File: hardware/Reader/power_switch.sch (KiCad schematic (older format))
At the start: 9 parts

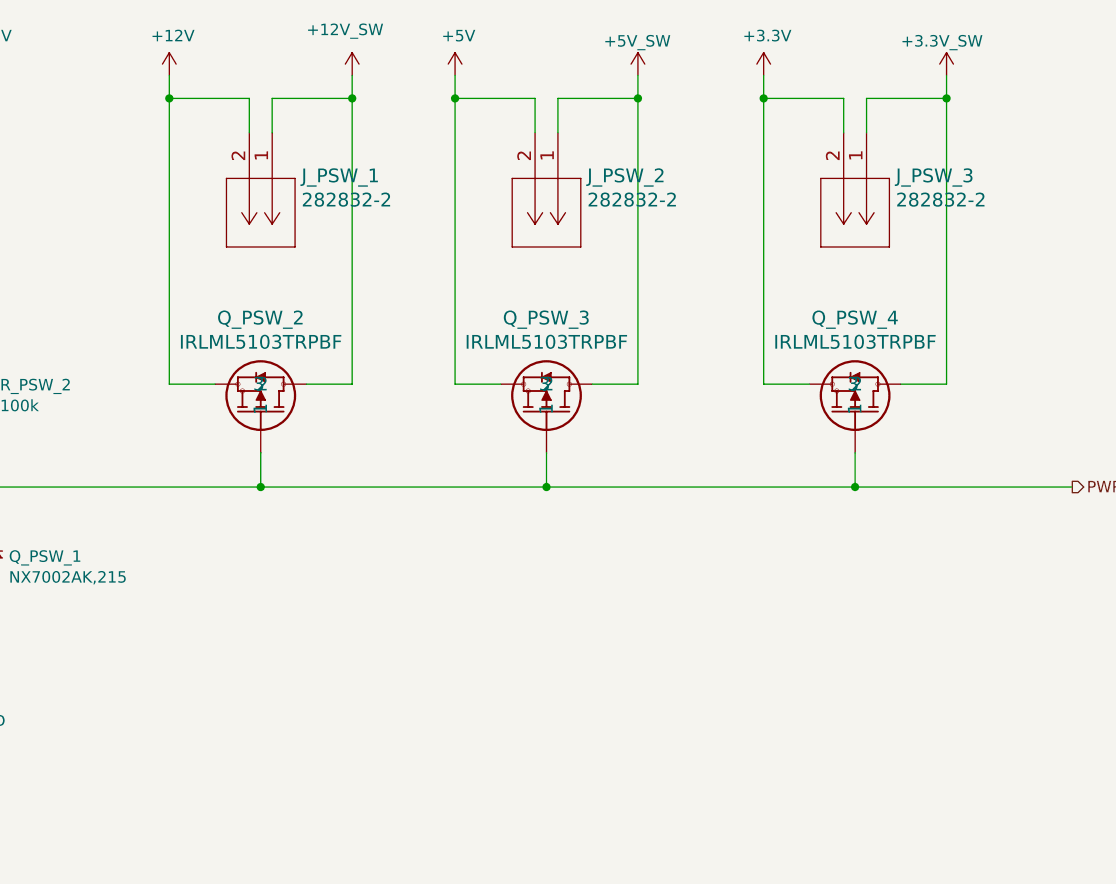
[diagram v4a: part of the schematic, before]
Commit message: Fixed bugs on the reader schematic. Exported Schematic Electrical report
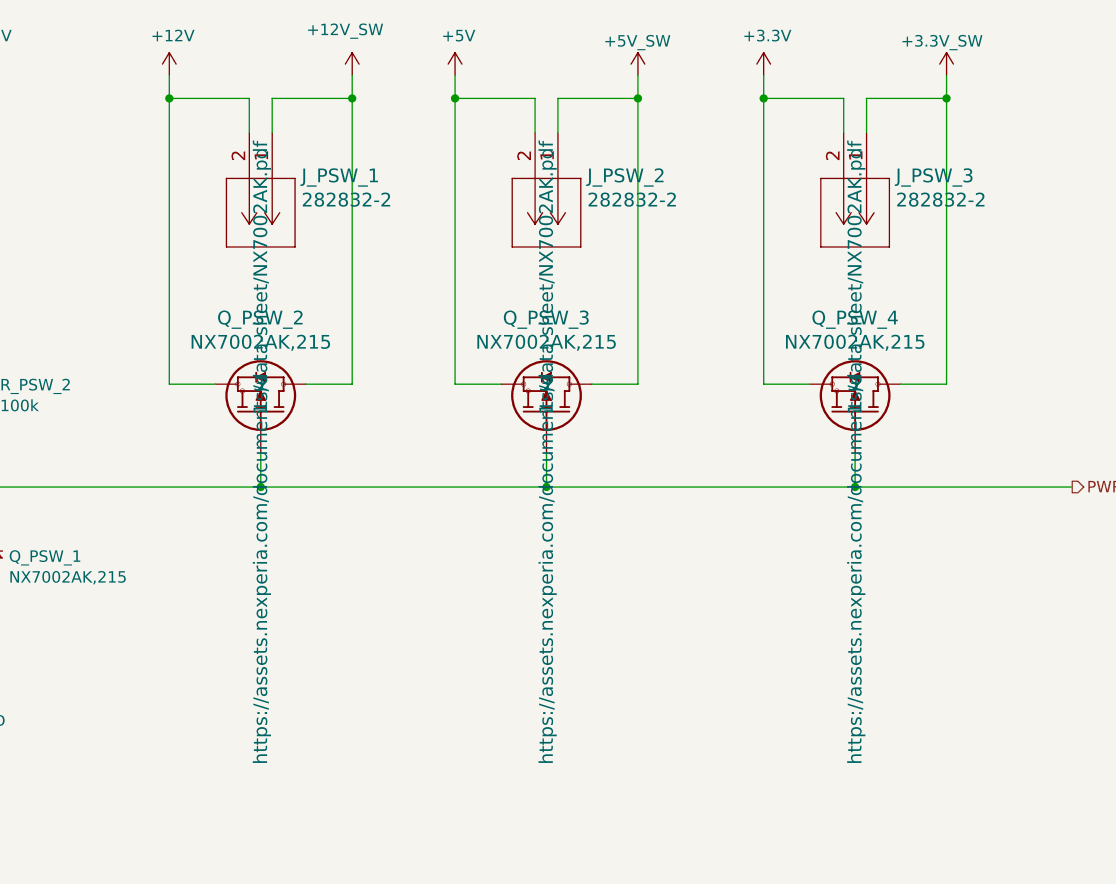
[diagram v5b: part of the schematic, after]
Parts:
- J_PSW_1, J_PSW_2, J_PSW_3: Manufacturer (none) -> TE Connectivity AMP Connectors; Vendor (none) -> DigiKey Canada; digikeypn (none) -> A113314-ND
- Q_PSW_1: Manufacturer (none) -> Nexperia USA Inc.; Part Name (none) -> NX7002AK,215; Vendor (none) -> DigiKey Canada; digikeypn (none) -> 1727-1289-1-ND
- Q_PSW_2, Q_PSW_3, Q_PSW_4: value IRLML5103TRPBF -> NX7002AK,215; footprint footprints:IRLML5103TRPBF -> footprints:SOT95P230X110-3N; Manufacturer (none) -> Nexperia USA Inc.; Part Name (none) -> NX7002AK,215; Vendor (none) -> DigiKey Canada; digikeypn (none) -> 1727-1289-1-ND
- R_PSW_1, R_PSW_2: Manufacturer (none) -> Yageo; Vendor (none) -> DigiKey Canada; digikeypn (none) -> 311-2395-1-ND
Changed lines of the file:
@@
 AR Path="/5FA56A4E/5FA57921" Ref="Q_PSW_3"  Part="1"
 F 0 "Q_PSW_3" V 6489 3500 60  0000 C CNN
-F 1 "IRLML5103TRPBF" V 6383 3500 60  0000 C CNN
-F 2 "footprints:IRLML5103TRPBF" H 6350 3240 60  0001 C CNN
-F 3 "" H 5900 3500 60  0000 C CNN
+F 1 "NX7002AK,215" V 6383 3500 60  0000 C CNN
+F 2 "footprints:SOT95P230X110-3N" H 6350 3240 60  0001 C CNN
+F 3 "https://assets.nexperia.com/documents/data-sheet/NX7002AK.pdf" H 5900 3500 60  0000 C CNN
+F 4 "NX7002AK,215" H 5900 3500 50  0001 C CNN "Part Name"
+F 5 "Nexperia USA Inc." H 5900 3500 50  0001 C CNN "Manufacturer"
+F 6 "DigiKey Canada" H 5900 3500 50  0001 C CNN "Vendor"
+F 7 "1727-1289-1-ND" H 5900 3500 50  0001 C CNN "digikeypn"
 	1    5900 3500
 	0    1    -1   0
@@
 AR Path="/5FA56A4E/5FA57927" Ref="Q_PSW_4"  Part="1"
 F 0 "Q_PSW_4" V 7839 3500 60  0000 C CNN
-F 1 "IRLML5103TRPBF" V 7733 3500 60  0000 C CNN
-F 2 "footprints:IRLML5103TRPBF" H 7700 3240 60  0001 C CNN
-F 3 "" H 7250 3500 60  0000 C CNN
+F 1 "NX7002AK,215" V 7733 3500 60  0000 C CNN
+F 2 "footprints:SOT95P230X110-3N" H 7700 3240 60  0001 C CNN
+F 3 "https://assets.nexperia.com/documents/data-sheet/NX7002AK.pdf" H 7250 3500 60  0000 C CNN
+F 4 "NX7002AK,215" H 7250 3500 50  0001 C CNN "Part Name"
+F 5 "Nexperia USA Inc." H 7250 3500 50  0001 C CNN "Manufacturer"
+F 6 "DigiKey Canada" H 7250 3500 50  0001 C CNN "Vendor"
+F 7 "1727-1289-1-ND" H 7250 3500 50  0001 C CNN "digikeypn"
 	1    7250 3500
 	0    1    -1   0
@@
 F 5 "7" H 3350 3950 50  0001 L BNN "Field5"
 F 6 "IPC-7351B" H 3350 3950 50  0001 L BNN "Field6"
+F 7 "NX7002AK,215" H 3350 3950 50  0001 C CNN "Part Name"
+F 8 "Nexperia USA Inc." H 3350 3950 50  0001 C CNN "Manufacturer"
+F 9 "DigiKey Canada" H 3350 3950 50  0001 C CNN "Vendor"
+F 10 "1727-1289-1-ND" H 3350 3950 50  0001 C CNN "digikeypn"
 	1    3350 3950
 	1    0    0    -1
@@
 F 1 "100k" H 3509 3205 50  0000 L CNN
 F 2 "footprints:RESC1608X55N" H 3450 3250 50  0001 C CNN
-F 3 "https://assets.nexperia.com/documents/data-sheet/NX7002AK.pdf" H 3450 3250 50  0001 C CNN
+F 3 "https://www.yageo.com/upload/media/product/productsearch/datasheet/rchip/PYu-RT_1-to-0.01_RoHS_L_12.pdf" H 3450 3250 50  0001 C CNN
 F 4 "RT0603DRE07100KL" H 3450 3250 50  0001 C CNN "Part Name"
+F 5 "Yageo" H 3450 3250 50  0001 C CNN "Manufacturer"
+F 6 "DigiKey Canada" H 3450 3250 50  0001 C CNN "Vendor"
+F 7 "311-2395-1-ND" H 3450 3250 50  0001 C CNN "digikeypn"
 	1    3450 3250
 	1    0    0    -1
@@
 F 1 "100k" H 2409 3505 50  0000 L CNN
 F 2 "footprints:RESC1608X55N" H 2350 3550 50  0001 C CNN
-F 3 "https://assets.nexperia.com/documents/data-sheet/NX7002AK.pdf" H 2350 3550 50  0001 C CNN
+F 3 "https://www.yageo.com/upload/media/product/productsearch/datasheet/rchip/PYu-RT_1-to-0.01_RoHS_L_12.pdf" H 2350 3550 50  0001 C CNN
 F 4 "RT0603DRE07100KL" H 2350 3550 50  0001 C CNN "Part Name"
+F 5 "Yageo" H 2350 3550 50  0001 C CNN "Manufacturer"
+F 6 "DigiKey Canada" H 2350 3550 50  0001 C CNN "Vendor"
+F 7 "311-2395-1-ND" H 2350 3550 50  0001 C CNN "digikeypn"
 	1    2350 3550
 	1    0    0    -1
@@
 AR Path="/5FA56A4E/5FA5791B" Ref="Q_PSW_2"  Part="1"
 F 0 "Q_PSW_2" V 5239 3500 60  0000 C CNN
-F 1 "IRLML5103TRPBF" V 5133 3500 60  0000 C CNN
-F 2 "footprints:IRLML5103TRPBF" H 5100 3240 60  0001 C CNN
-F 3 "" H 4650 3500 60  0000 C CNN
+F 1 "NX7002AK,215" V 5133 3500 60  0000 C CNN
+F 2 "footprints:SOT95P230X110-3N" H 5100 3240 60  0001 C CNN
+F 3 "https://assets.nexperia.com/documents/data-sheet/NX7002AK.pdf" H 4650 3500 60  0000 C CNN
+F 4 "NX7002AK,215" H 4650 3500 50  0001 C CNN "Part Name"
+F 5 "Nexperia USA Inc." H 4650 3500 50  0001 C CNN "Manufacturer"
+F 6 "DigiKey Canada" H 4650 3500 50  0001 C CNN "Vendor"
+F 7 "1727-1289-1-ND" H 4650 3500 50  0001 C CNN "digikeypn"
 	1    4650 3500
 	0    1    -1   0
@@
 F 3 "https://www.te.com/commerce/DocumentDelivery/DDEController?Action=srchrtrv&DocNm=282832&DocType=Customer+Drawing&DocLang=English" H 4700 2100 60  0001 C CNN
 F 4 "282832-2" H 4700 2100 50  0001 C CNN "Part Name"
+F 5 "DigiKey Canada" H 4700 2100 50  0001 C CNN "Vendor"
+F 6 "TE Connectivity AMP Connectors" H 4700 2100 50  0001 C CNN "Manufacturer"
+F 7 "A113314-ND" H 4700 2100 50  0001 C CNN "digikeypn"
 	1    4700 2100
 	0    1    1    0
@@
 F 3 "https://www.te.com/commerce/DocumentDelivery/DDEController?Action=srchrtrv&DocNm=282832&DocType=Customer+Drawing&DocLang=English" H 5950 2100 60  0001 C CNN
 F 4 "282832-2" H 5950 2100 50  0001 C CNN "Part Name"
+F 5 "DigiKey Canada" H 5950 2100 50  0001 C CNN "Vendor"
+F 6 "TE Connectivity AMP Connectors" H 5950 2100 50  0001 C CNN "Manufacturer"
+F 7 "A113314-ND" H 5950 2100 50  0001 C CNN "digikeypn"
 	1    5950 2100
 	0    1    1    0
@@
 F 3 "https://www.te.com/commerce/DocumentDelivery/DDEController?Action=srchrtrv&DocNm=282832&DocType=Customer+Drawing&DocLang=English" H 7300 2100 60  0001 C CNN
 F 4 "282832-2" H 7300 2100 50  0001 C CNN "Part Name"
+F 5 "DigiKey Canada" H 7300 2100 50  0001 C CNN "Vendor"
+F 6 "TE Connectivity AMP Connectors" H 7300 2100 50  0001 C CNN "Manufacturer"
+F 7 "A113314-ND" H 7300 2100 50  0001 C CNN "digikeypn"
 	1    7300 2100
 	0    1    1    0

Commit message: Fixed bugs in schematic. Updated BOM list. Swapped to using ESP32 holder. Updated PCB layout to v0.0.2. Updated schematic to v0.0.4
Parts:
- J_PSW_1, J_PSW_2, J_PSW_3: value 282832-2 -> 1546931-2; footprint footprints:282832-2 -> footprints:1546931-2; symbol 2828322:282832-2 -> Reader-rescue:282832-2-2828322; Part Name 282832-2 -> 1546931-2; digikeypn A113314-ND -> A97965-ND
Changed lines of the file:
@@
 Sheet 2 19
 Title "CANnect Reader | Power Switch"
-Date "2020-10-27"
-Rev "0.0.03"
+Date "2020-10-28"
+Rev "0.0.04"
 Comp "CANtech"
 Comment1 "Created by Choong Jin Ng | jin8383@gmail.com"
@@
 F 1 "NX7002AK,215" V 6383 3500 60  0000 C CNN
 F 2 "footprints:SOT95P230X110-3N" H 6350 3240 60  0001 C CNN
-F 3 "https://assets.nexperia.com/documents/data-sheet/NX7002AK.pdf" H 5900 3500 60  0000 C CNN
+F 3 "https://assets.nexperia.com/documents/data-sheet/NX7002AK.pdf" H 5900 3500 60  0001 C CNN
 F 4 "NX7002AK,215" H 5900 3500 50  0001 C CNN "Part Name"
 F 5 "Nexperia USA Inc." H 5900 3500 50  0001 C CNN "Manufacturer"
@@
 F 1 "NX7002AK,215" V 7733 3500 60  0000 C CNN
 F 2 "footprints:SOT95P230X110-3N" H 7700 3240 60  0001 C CNN
-F 3 "https://assets.nexperia.com/documents/data-sheet/NX7002AK.pdf" H 7250 3500 60  0000 C CNN
+F 3 "https://assets.nexperia.com/documents/data-sheet/NX7002AK.pdf" H 7250 3500 60  0001 C CNN
 F 4 "NX7002AK,215" H 7250 3500 50  0001 C CNN "Part Name"
 F 5 "Nexperia USA Inc." H 7250 3500 50  0001 C CNN "Manufacturer"
@@
 F 1 "NX7002AK,215" V 5133 3500 60  0000 C CNN
 F 2 "footprints:SOT95P230X110-3N" H 5100 3240 60  0001 C CNN
-F 3 "https://assets.nexperia.com/documents/data-sheet/NX7002AK.pdf" H 4650 3500 60  0000 C CNN
+F 3 "https://assets.nexperia.com/documents/data-sheet/NX7002AK.pdf" H 4650 3500 60  0001 C CNN
 F 4 "NX7002AK,215" H 4650 3500 50  0001 C CNN "Part Name"
 F 5 "Nexperia USA Inc." H 4650 3500 50  0001 C CNN "Manufacturer"
@@
 Connection ~ 7250 3650
 $Comp
-L 2828322:282832-2 J_PSW_1
+L Reader-rescue:282832-2-2828322 J_PSW_1
 U 1 1 5F9A0984
 P 4700 2100
+AR Path="/5F9A0984" Ref="J_PSW_1"  Part="1"
+AR Path="/5FA56A4E/5F9A0984" Ref="J_PSW_1"  Part="1"
 F 0 "J_PSW_1" V 4889 2228 60  0000 L CNN
-F 1 "282832-2" V 4995 2228 60  0000 L CNN
-F 2 "footprints:282832-2" H 5100 2040 60  0001 C CNN
-F 3 "https://www.te.com/commerce/DocumentDelivery/DDEController?Action=srchrtrv&DocNm=282832&DocType=Customer+Drawing&DocLang=English" H 4700 2100 60  0001 C CNN
-F 4 "282832-2" H 4700 2100 50  0001 C CNN "Part Name"
+F 1 "1546931-2" V 4995 2228 60  0000 L CNN
+F 2 "footprints:1546931-2" H 5100 2040 60  0001 C CNN
+F 3 "https://www.te.com/commerce/DocumentDelivery/DDEController?Action=srchrtrv&DocNm=1-1773458-1_EURO_STYLE_QRG&DocType=DS&DocLang=English" H 4700 2100 60  0001 C CNN
+F 4 "1546931-2" H 4700 2100 50  0001 C CNN "Part Name"
 F 5 "DigiKey Canada" H 4700 2100 50  0001 C CNN "Vendor"
 F 6 "TE Connectivity AMP Connectors" H 4700 2100 50  0001 C CNN "Manufacturer"
-F 7 "A113314-ND" H 4700 2100 50  0001 C CNN "digikeypn"
+F 7 "A97965-ND" H 4700 2100 50  0001 C CNN "digikeypn"
 	1    4700 2100
 	0    1    1    0
@@
 $EndComp
 $Comp
-L 2828322:282832-2 J_PSW_2
+L Reader-rescue:282832-2-2828322 J_PSW_2
 U 1 1 5F9A6466
 P 5950 2100
+AR Path="/5F9A6466" Ref="J_PSW_2"  Part="1"
+AR Path="/5FA56A4E/5F9A6466" Ref="J_PSW_2"  Part="1"
 F 0 "J_PSW_2" V 6139 2228 60  0000 L CNN
-F 1 "282832-2" V 6245 2228 60  0000 L CNN
-F 2 "footprints:282832-2" H 6350 2040 60  0001 C CNN
-F 3 "https://www.te.com/commerce/DocumentDelivery/DDEController?Action=srchrtrv&DocNm=282832&DocType=Customer+Drawing&DocLang=English" H 5950 2100 60  0001 C CNN
-F 4 "282832-2" H 5950 2100 50  0001 C CNN "Part Name"
+F 1 "1546931-2" V 6245 2228 60  0000 L CNN
+F 2 "footprints:1546931-2" H 6350 2040 60  0001 C CNN
+F 3 "https://www.te.com/commerce/DocumentDelivery/DDEController?Action=srchrtrv&DocNm=1-1773458-1_EURO_STYLE_QRG&DocType=DS&DocLang=English" H 5950 2100 60  0001 C CNN
+F 4 "1546931-2" H 5950 2100 50  0001 C CNN "Part Name"
 F 5 "DigiKey Canada" H 5950 2100 50  0001 C CNN "Vendor"
 F 6 "TE Connectivity AMP Connectors" H 5950 2100 50  0001 C CNN "Manufacturer"
-F 7 "A113314-ND" H 5950 2100 50  0001 C CNN "digikeypn"
+F 7 "A97965-ND" H 5950 2100 50  0001 C CNN "digikeypn"
 	1    5950 2100
 	0    1    1    0
 $EndComp
 $Comp
-L 2828322:282832-2 J_PSW_3
+L Reader-rescue:282832-2-2828322 J_PSW_3
 U 1 1 5F9A673F
 P 7300 2100
+AR Path="/5F9A673F" Ref="J_PSW_3"  Part="1"
+AR Path="/5FA56A4E/5F9A673F" Ref="J_PSW_3"  Part="1"
 F 0 "J_PSW_3" V 7489 2228 60  0000 L CNN
-F 1 "282832-2" V 7595 2228 60  0000 L CNN
-F 2 "footprints:282832-2" H 7700 2040 60  0001 C CNN
-F 3 "https://www.te.com/commerce/DocumentDelivery/DDEController?Action=srchrtrv&DocNm=282832&DocType=Customer+Drawing&DocLang=English" H 7300 2100 60  0001 C CNN
-F 4 "282832-2" H 7300 2100 50  0001 C CNN "Part Name"
+F 1 "1546931-2" V 7595 2228 60  0000 L CNN
+F 2 "footprints:1546931-2" H 7700 2040 60  0001 C CNN
+F 3 "https://www.te.com/commerce/DocumentDelivery/DDEController?Action=srchrtrv&DocNm=1-1773458-1_EURO_STYLE_QRG&DocType=DS&DocLang=English" H 7300 2100 60  0001 C CNN
+F 4 "1546931-2" H 7300 2100 50  0001 C CNN "Part Name"
 F 5 "DigiKey Canada" H 7300 2100 50  0001 C CNN "Vendor"
 F 6 "TE Connectivity AMP Connectors" H 7300 2100 50  0001 C CNN "Manufacturer"
-F 7 "A113314-ND" H 7300 2100 50  0001 C CNN "digikeypn"
+F 7 "A97965-ND" H 7300 2100 50  0001 C CNN "digikeypn"
 	1    7300 2100
 	0    1    1    0
